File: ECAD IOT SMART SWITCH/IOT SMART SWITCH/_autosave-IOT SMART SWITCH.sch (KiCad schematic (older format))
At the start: 43 parts, among them J1 Conn_02x02_Odd_Even, J2 Conn_02x02_Odd_Even, J3 Conn_02x02_Odd_Even, J4 Conn_01x20, J5 Conn_01x20, J6 Conn_02x02_Odd_Even, J7 Conn_02x02_Odd_Even, K1 SLA-12VDC-SL, Q1 BS170, T1 VC 10/1/18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

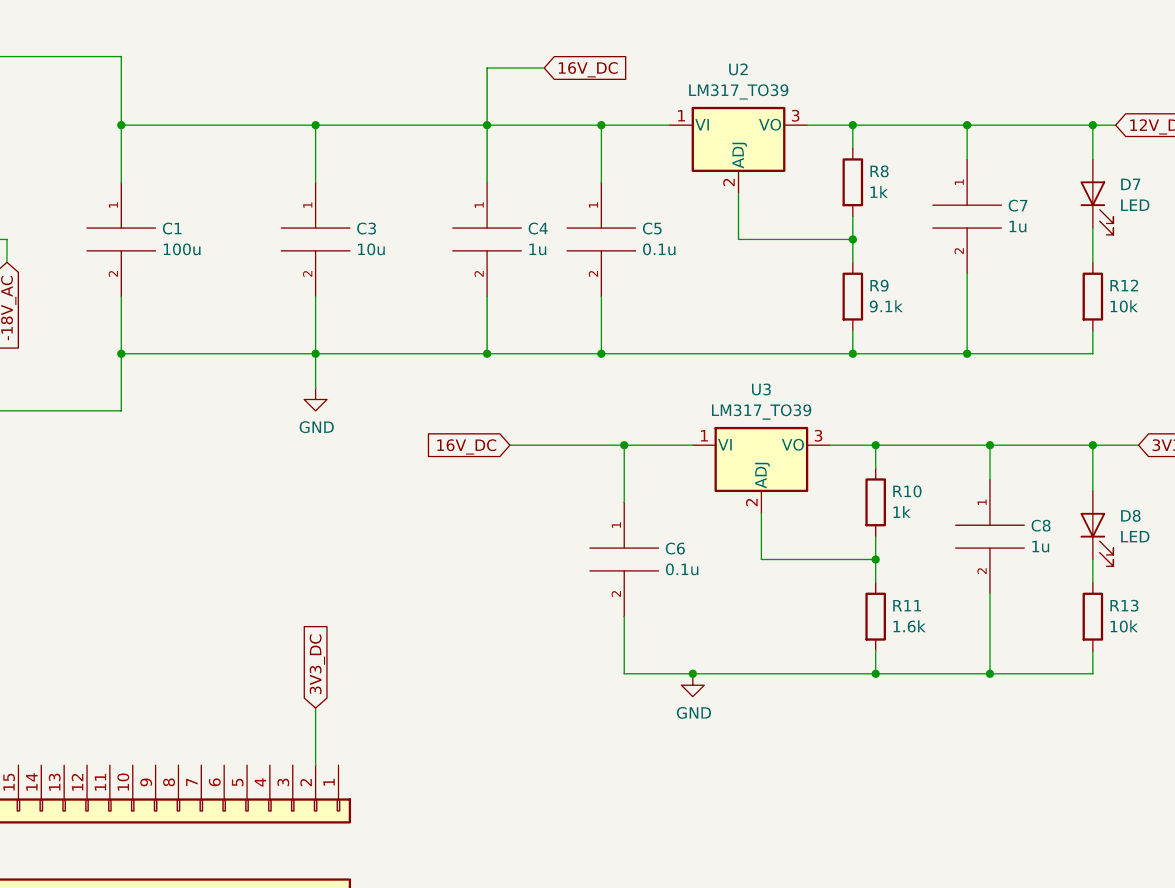
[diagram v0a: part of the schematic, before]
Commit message: Not within budget
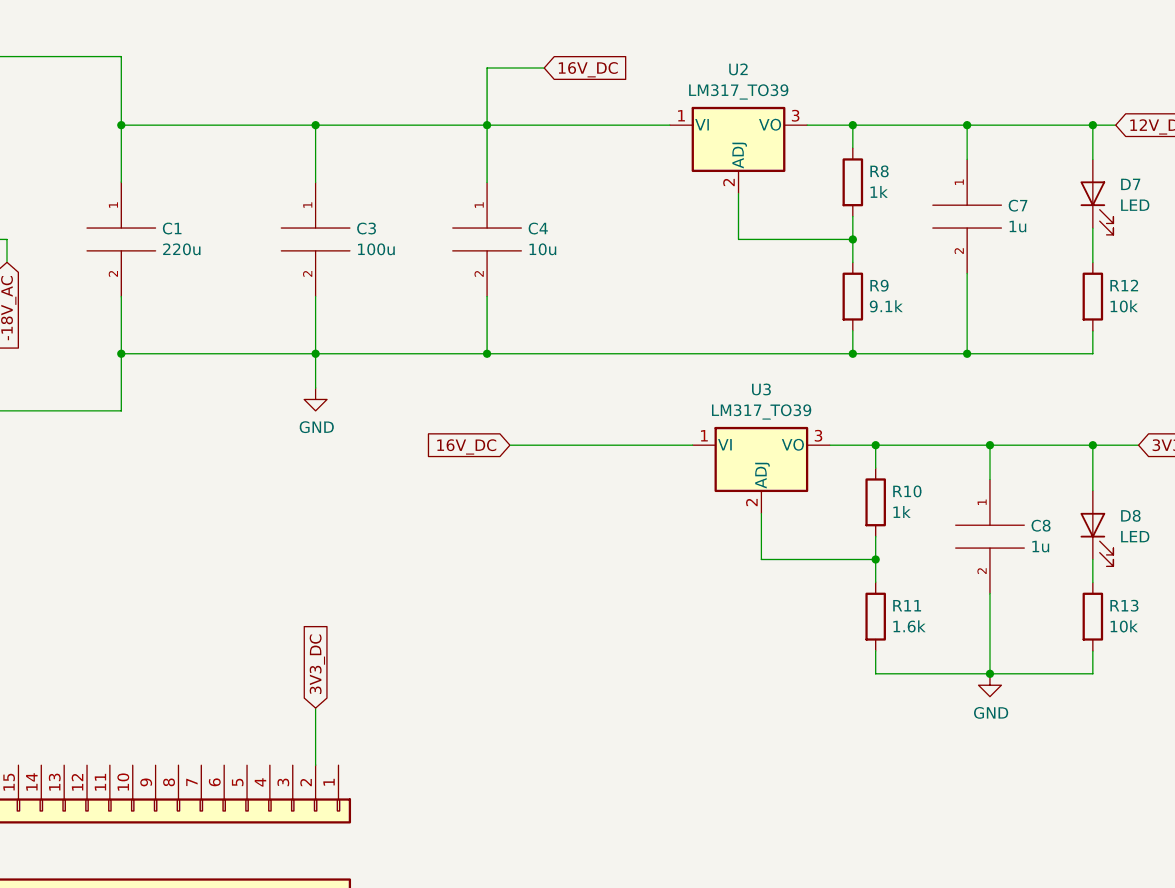
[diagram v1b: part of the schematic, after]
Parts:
- removed C5, C6: 0.1u, symbol pspice:C
- C1: value 100u -> 220u
- C3: value 10u -> 100u
- C4: value 1u -> 10u
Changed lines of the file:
@@
 P 6200 1450
 F 0 "C1" H 6378 1496 50  0000 L CNN
-F 1 "100u" H 6378 1405 50  0000 L CNN
+F 1 "220u" H 6378 1405 50  0000 L CNN
 F 2 "" H 6200 1450 50  0001 C CNN
 F 3 "~" H 6200 1450 50  0001 C CNN
@@
 P 7050 1450
 F 0 "C3" H 7228 1496 50  0000 L CNN
-F 1 "10u" H 7228 1405 50  0000 L CNN
+F 1 "100u" H 7228 1405 50  0000 L CNN
 F 2 "" H 7050 1450 50  0001 C CNN
 F 3 "~" H 7050 1450 50  0001 C CNN
@@
 P 7800 1450
 F 0 "C4" H 7978 1496 50  0000 L CNN
-F 1 "1u" H 7978 1405 50  0000 L CNN
+F 1 "10u" H 7978 1405 50  0000 L CNN
 F 2 "" H 7800 1450 50  0001 C CNN
 F 3 "~" H 7800 1450 50  0001 C CNN
@@
 Wire Wire Line
 	9900 1600 9900 1950
-$Comp
-L pspice:C C5
-U 1 1 60AFCF29
-P 8300 1450
-F 0 "C5" H 8478 1496 50  0000 L CNN
-F 1 "0.1u" H 8478 1405 50  0000 L CNN
-F 2 "" H 8300 1450 50  0001 C CNN
-F 3 "~" H 8300 1450 50  0001 C CNN
-	1    8300 1450
-	1    0    0    -1
-$EndComp
-Wire Wire Line
-	8300 1200 8300 950
-Wire Wire Line
-	8300 950  7800 950
-Wire Wire Line
-	8300 1700 8300 1950
-Connection ~ 8300 950
-Wire Wire Line
-	8600 950  8300 950
-Wire Wire Line
-	8300 1950 9400 1950
 Wire Wire Line
 	9900 1100 9900 950
@@
 Wire Wire Line
 	7050 2100 7050 1950
-Wire Wire Line
-	8300 1950 7800 1950
-Connection ~ 8300 1950
 Connection ~ 7800 1950
 Wire Wire Line
@@
 Wire Wire Line
 	10000 3000 10000 3350
-$Comp
-L pspice:C C6
-U 1 1 60D2A1DC
-P 8400 2850
-F 0 "C6" H 8578 2896 50  0000 L CNN
-F 1 "0.1u" H 8578 2805 50  0000 L CNN
-F 2 "" H 8400 2850 50  0001 C CNN
-F 3 "~" H 8400 2850 50  0001 C CNN
-	1    8400 2850
-	1    0    0    -1
-$EndComp
-Wire Wire Line
-	8400 2600 8400 2350
-Wire Wire Line
-	8400 2350 7900 2350
-Wire Wire Line
-	8400 3100 8400 3350
-Connection ~ 8400 2350
-Wire Wire Line
-	8700 2350 8400 2350
-Wire Wire Line
-	8400 3350 8700 3350
 Wire Wire Line
 	10000 2500 10000 2350
@@
 Wire Wire Line
 	9500 3250 9500 3350
-Connection ~ 9500 3350
 Text GLabel 10650 2350 2    50   Input ~ 0
 3V3_DC
@@
 L power:GND #PWR08
 U 1 1 60D61A25
-P 8700 3350
-F 0 "#PWR08" H 8700 3100 50  0001 C CNN
-F 1 "GND" H 8705 3177 50  0000 C CNN
-F 2 "" H 8700 3350 50  0001 C CNN
-F 3 "" H 8700 3350 50  0001 C CNN
-	1    8700 3350
-	1    0    0    -1
-$EndComp
-Connection ~ 8700 3350
-Wire Wire Line
-	8700 3350 9500 3350
+P 10000 3350
+F 0 "#PWR08" H 10000 3100 50  0001 C CNN
+F 1 "GND" H 10005 3177 50  0000 C CNN
+F 2 "" H 10000 3350 50  0001 C CNN
+F 3 "" H 10000 3350 50  0001 C CNN
+	1    10000 3350
+	1    0    0    -1
+$EndComp
 $Comp
 L Device:LED D8
@@
 	1    0    0    -1
 $EndComp
+Wire Wire Line
+	7800 950  8600 950
+Wire Wire Line
+	7800 1950 9400 1950
+Wire Wire Line
+	7900 2350 8700 2350
 $EndSCHEMATC
